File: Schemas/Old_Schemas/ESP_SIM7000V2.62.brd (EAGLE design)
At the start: 89.7 x 57.9 mm, 77 parts, among them J1 U.FL-R-SMT(01), J2 U.FL-R-SMT(01), J3 78646-3001, Q1 SI2305CDS, Q2 BSS138, Q3 SI2305CDS, Q4 BSS138, Q5 SI2305CDS, Q6 BSS138, Q7 BSS138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

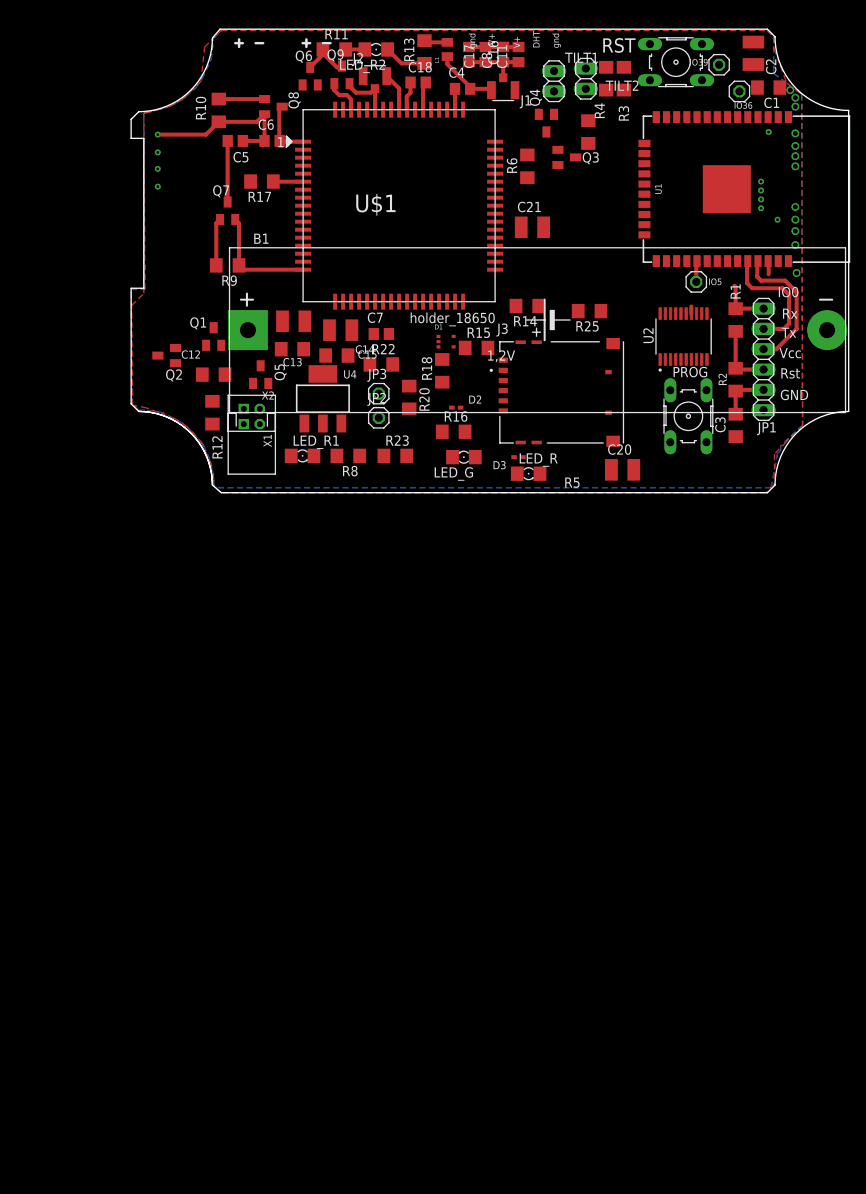
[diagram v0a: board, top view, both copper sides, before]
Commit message: Mouvement, voiture aléatoires, deux types de NPC...
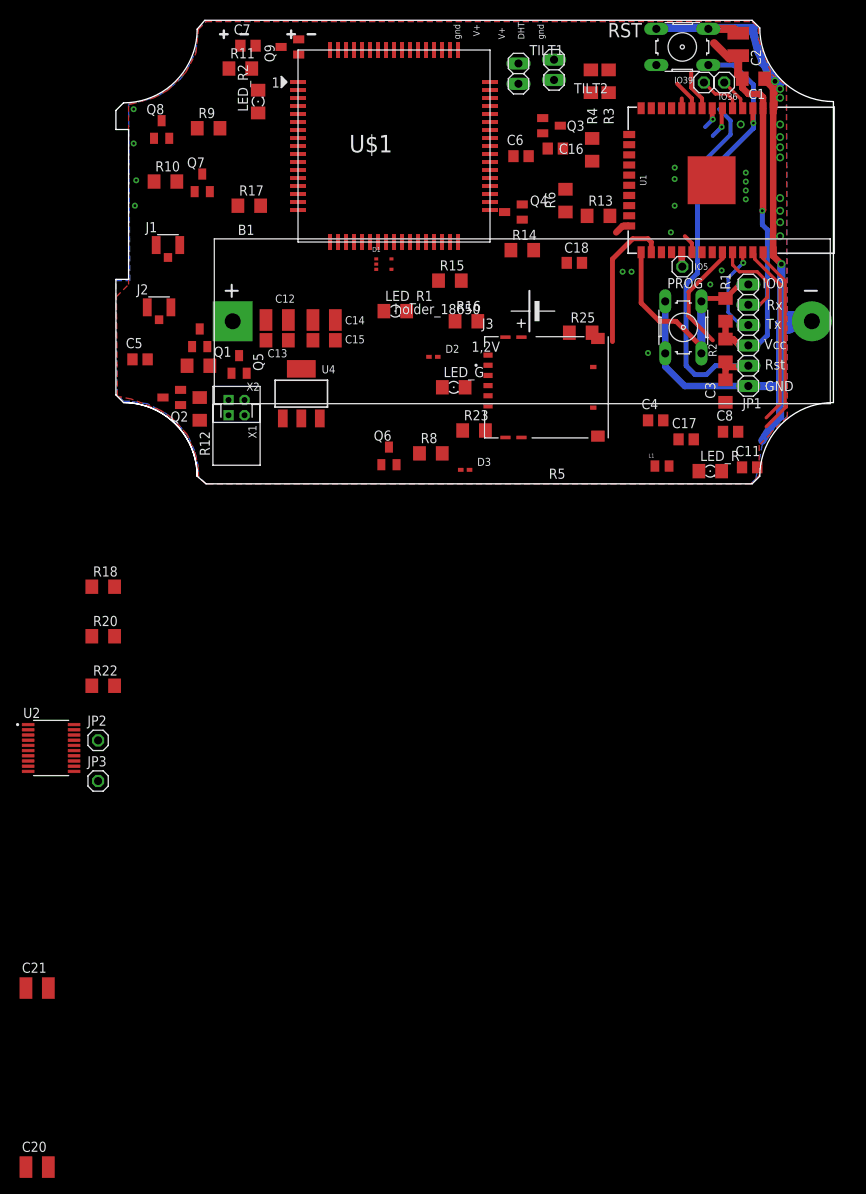
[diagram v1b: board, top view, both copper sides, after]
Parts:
- C5, C6: value 100nF -> 100uF
- moved C20 113.8 mm to (-7.78, -83.8)
- moved C21 113.5 mm to (-7.78, -61.4)
- moved U2 94.3 mm to (-6.03, -31.4), turned to 0 degrees
- moved JP3 59.8 mm to (-0.16, -35.6)
- moved C11 59.1 mm to (81.3, 3.65), turned to 0 degrees
- moved L1 58.6 mm to (70.3, 3.81), turned to 0 degrees
- moved C8 55.1 mm to (78.9, 8.10), turned to 0 degrees
- moved C17 54.2 mm to (73.3, 7.14), turned to 0 degrees
- moved JP2 53.4 mm to (-0.16, -30.5)
- moved R22 53.1 mm to (0.48, -23.7)
- moved R18 50.2 mm to (0.48, -11.3), turned to 0 degrees
- moved R20 48.5 mm to (0.48, -17.5), turned to 0 degrees
- moved Q6 48.5 mm to (36.2, 5.08)
- moved C4 47.9 mm to (69.5, 9.53)
- moved J1 46.2 mm to (8.57, 31.4), turned to 0 degrees
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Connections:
- removed net N$32: JP2.1, R20.2
- new net +5V: C20.2, U2.19
- new net N$15: LED_R1.A
- new net N$18: R10.2
- new net N$19: C11.2, C16.2, C17.2, C8.2
- new net N$20: C5.1
- new net N$22: Q7.2, R9.1
- new net N$23: R9.2
- new net N$25: Q8.2, R10.1
- new net N$27: C6.2
- new net N$29: D2.2
- new net N$30: C6.1
- new net N$31: D2.1
- new net N$35: C18.2, R13.1
- new net N$43: R22.2
- new net N$44: U$1.P$34
- new net N$9: D3.2
- net +3V3: no longer C20.2, U2.19
- net GND: now also LED_R2.A, U$1.P$55, U$1.P$56, U$1.P$57; no longer C5.1, C6.1, D2.2, D3.2, Q7.2, Q8.2, R10.1, R9.1
- net N$34: now also R20.1; no longer R22.2, U$1.P$34
- net N$42: no longer R20.1
- net NRESET_OUT: no longer R9.2
- net PWRKEY_IN: no longer C6.2, D2.1
- net PWRKEY_OUT: no longer R10.2
- net V+: no longer C11.2, C16.2, C17.2, C18.2, C8.2, LED_R1.A, LED_R2.A, R13.1, U$1.P$55, U$1.P$56, U$1.P$57
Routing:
- net RST: track 6.45 -> 61.0 mm
- net GND: track 53.9 -> 99.9 mm, vias 20 -> 29
- net +3V3: track 8.17 -> 49.7 mm
- net POWER: track 0.00 -> 23.9 mm
- net IO0: track 6.43 -> 30.3 mm
- net UC_SCL: track 2.56 -> 22.8 mm
- net NEXT: track 0.00 -> 17.7 mm
- net V+: track 15.1 -> 0.00 mm
- net UC_SDA: track 0.00 -> 14.5 mm
- net N$4: track 8.16 -> 0.00 mm
- net MEASURE: track 0.00 -> 7.81 mm
- net N$6: track 7.63 -> 0.00 mm
- net PWRKEY_IN: track 7.42 -> 0.00 mm
- net TX: track 17.5 -> 11.5 mm, vias 0 -> 1
- net NRESET_OUT: track 5.92 -> 0.00 mm
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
